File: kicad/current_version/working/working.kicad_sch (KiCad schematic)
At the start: 16 parts, among them J1 scuath, J1 sws2880, J1 swsi1h, J2 scumcsm, U1 imsp10mpump21rs2227

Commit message: workings
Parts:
- removed J1: swsi1h, oomlout_oomp_part_footprints:swsi1h_electronic_switch_slide_2d54_header_single_pole_double_throw, symbol oomlout_oomp_part_symbols:swsi1h_electronic_switch_slide_2d54_header_single_pol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
- removed J1: scuath, oomlout_oomp_part_footprints:scuath_electronic_socket_usb_a_through_hole, symbol oomlout_oomp_part_symbols:scuath_electronic_socket_usb_a_through_hole
- removed J1: sws2880, oomlout_oomp_part_footprints:sws2880_electronic_switch_slide_2_8_mm_x_8_mm_x_1_4_single_pole_double_throw, symbol oomlout_oomp_part_symbols:sws2880_electronic_switch_slide_2_8_mm_x_8_mm_x_1_4_s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
- removed J2 (x2): scumcsm, oomlout_oomp_part_footprints:scumcsm_electronic_socket_usb_micro_surface_mount, symbol oomlout_oomp_part_symbols:scumcsm_electronic_socket_usb_micro_surface_mount
- removed U1: imsp10mpump21rs2227, oomlout_oomp_part_footprints:imsp10mpump21rs2227_electronic_ic_msop_10_multiplexer_usb_multiplexer_two_to_one_jiangsu_r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, symbol oomlout_oomp_part_symbols:imsp10mpump21rs2227_electronic_ic_msop_10_multiplexer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
- added CON1 (x2): scumcsm, oomlout_oomp_part_footprints:scumcsm_electronic_socket_usb_micro_surface_mount, symbol oomlout_oomp_part_symbols:scumcsm_electronic_socket_usb_micro_surface_mount
- added CON1: scuath, oomlout_oomp_part_footprints:scuath_electronic_socket_usb_a_through_hole, symbol oomlout_oomp_part_symbols:scuath_electronic_socket_usb_a_through_hole
- added IC1: imsp10mpump21rs2227, oomlout_oomp_part_footprints:imsp10mpump21rs2227_electronic_ic_msop_10_multiplexer_usb_multiplexer_two_to_one_jiangsu_r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, symbol oomlout_oomp_part_symbols:imsp10mpump21rs2227_electronic_ic_msop_10_multiplexer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
- added SW1: swsi1h, oomlout_oomp_part_footprints:swsi1h_electronic_switch_slide_2d54_header_single_pole_double_throw, symbol oomlout_oomp_part_symbols:swsi1h_electronic_switch_slide_2d54_header_single_pol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
- added SW1: sws2880, oomlout_oomp_part_footprints:sws2880_electronic_switch_slide_2_8_mm_x_8_mm_x_1_4_single_pole_double_throw, symbol oomlout_oomp_part_symbols:sws2880_electronic_switch_slide_2_8_mm_x_8_mm_x_1_4_s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
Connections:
- net +5V: now also CON1.1 (VBUS), CON1.1 (VBUS), CON1.1 (VBUS), IC1.1 (___v_plus), SW1.2 (B), SW1.2 (B)
- net GND: now also CON1.4 (GND), CON1.5 (GND), CON1.5 (GND), CON1.5 (Shield), CON1.6 (Shield), CON1.6 (Shield), IC1.5 (___gnd)
- net usb_negative_main: now also CON1.2 (D-), IC1.4 (___d_minus)
- net usb_negative_secondary_1: now also CON1.2 (D-), IC1.6 (___hsd1_minus)
- net usb_negative_secondary_2: now also CON1.2 (D-), IC1.8 (___hsd2_minus)
- net usb_positive_main: now also CON1.3 (D+), IC1.3 (___d_plus)
- net usb_positive_secondary_1: now also CON1.3 (D+), IC1.7 (___hsd1_plus)
- net usb_positive_secondary_2: now also CON1.3 (D+), IC1.9 (___hsd2_plus)
- net at R1.1: now also IC1.10 (___oe)
- net out_1 renamed select
- net select: now also IC1.2 (___s), SW1.1 (A), SW1.1 (A)
- new net slide_switch_out_2: SW1.3 (C), SW1.3 (C)
- new net usb_id_secondary_1: CON1.4 (ID)
- new net usb_id_secondary_2: CON1.4 (ID)
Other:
- note added: "connector_usb_a_through_hole"
- note added: "connector_usb_micro_surface_mount"
- note added: "ic_usb_multiplexer_msop_10_two_to_one_rs2227xn"
- note added: "logic-glue"
- note added: "main"
- note added: "mechanical_board_shape_oobb_plate_03_03"
- note added: "oomp logic glue"
- note added: "rs2227 select"
- note added: "secondary_1"
- note added: "secondary_2"
- note added: "switch_slide_single_pole_double_throw_2_8_mm_x_8_mm_x_1_4"
- note added: "usb_a"
- note added: "usb_micro"
- note removed: "name"
- note removed: "oomp glue"
- note removed: "usb_a_main"
- note removed: "usb_micro secondary_1"
- note removed: "usb_micro secondary_2"

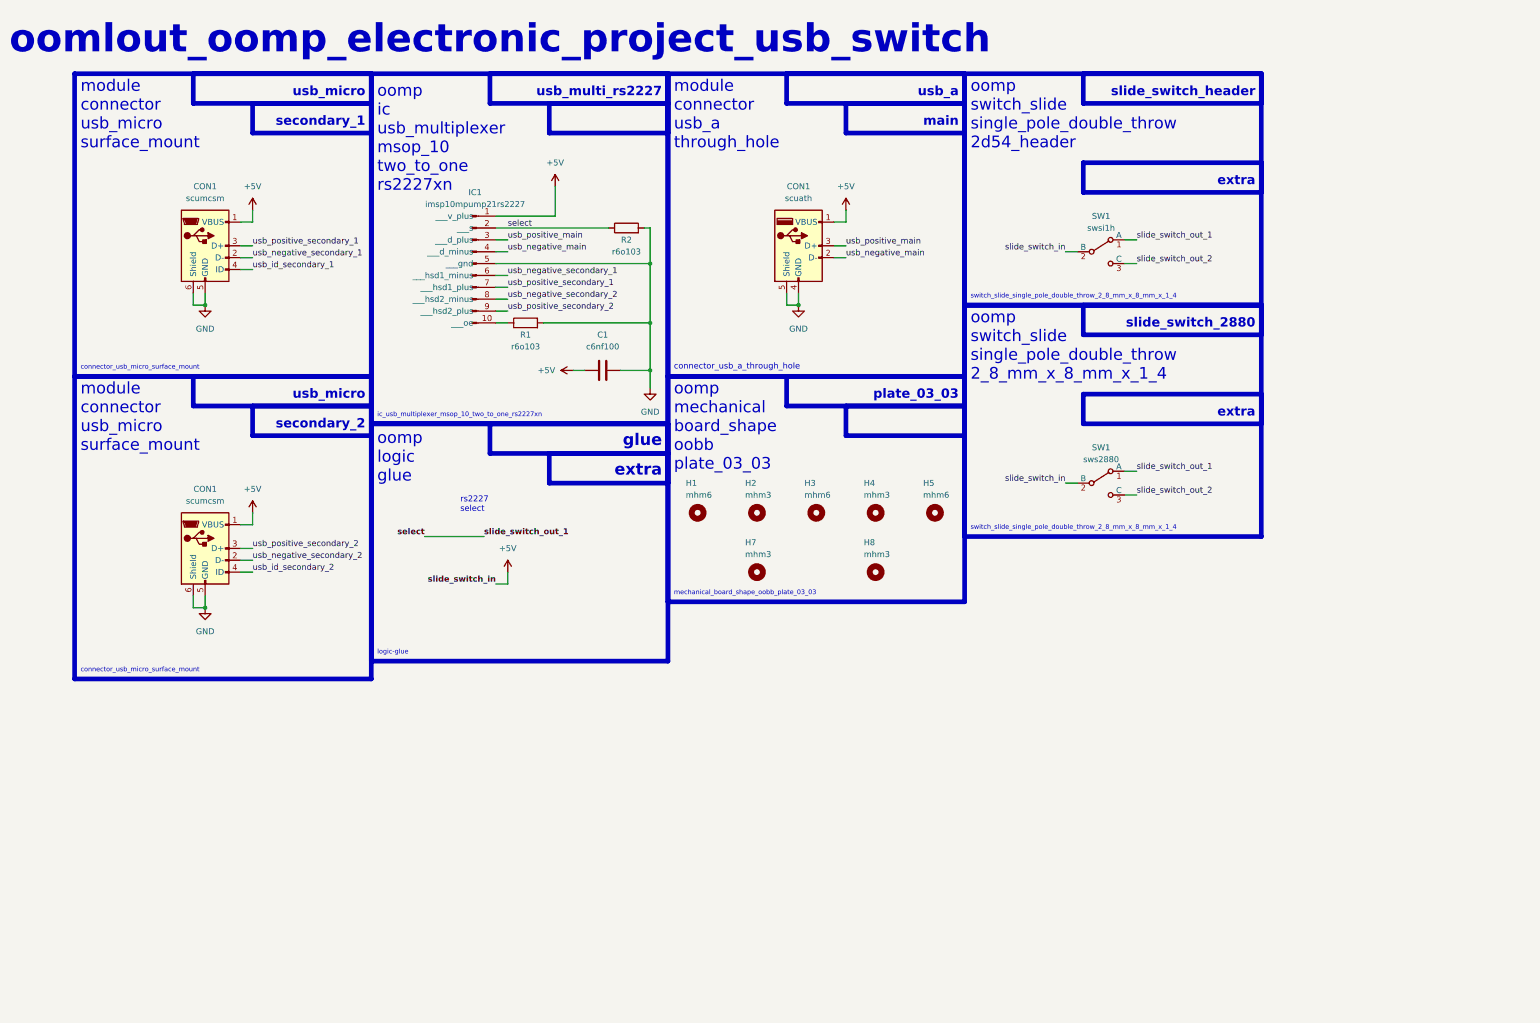
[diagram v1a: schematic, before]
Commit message: added power mux
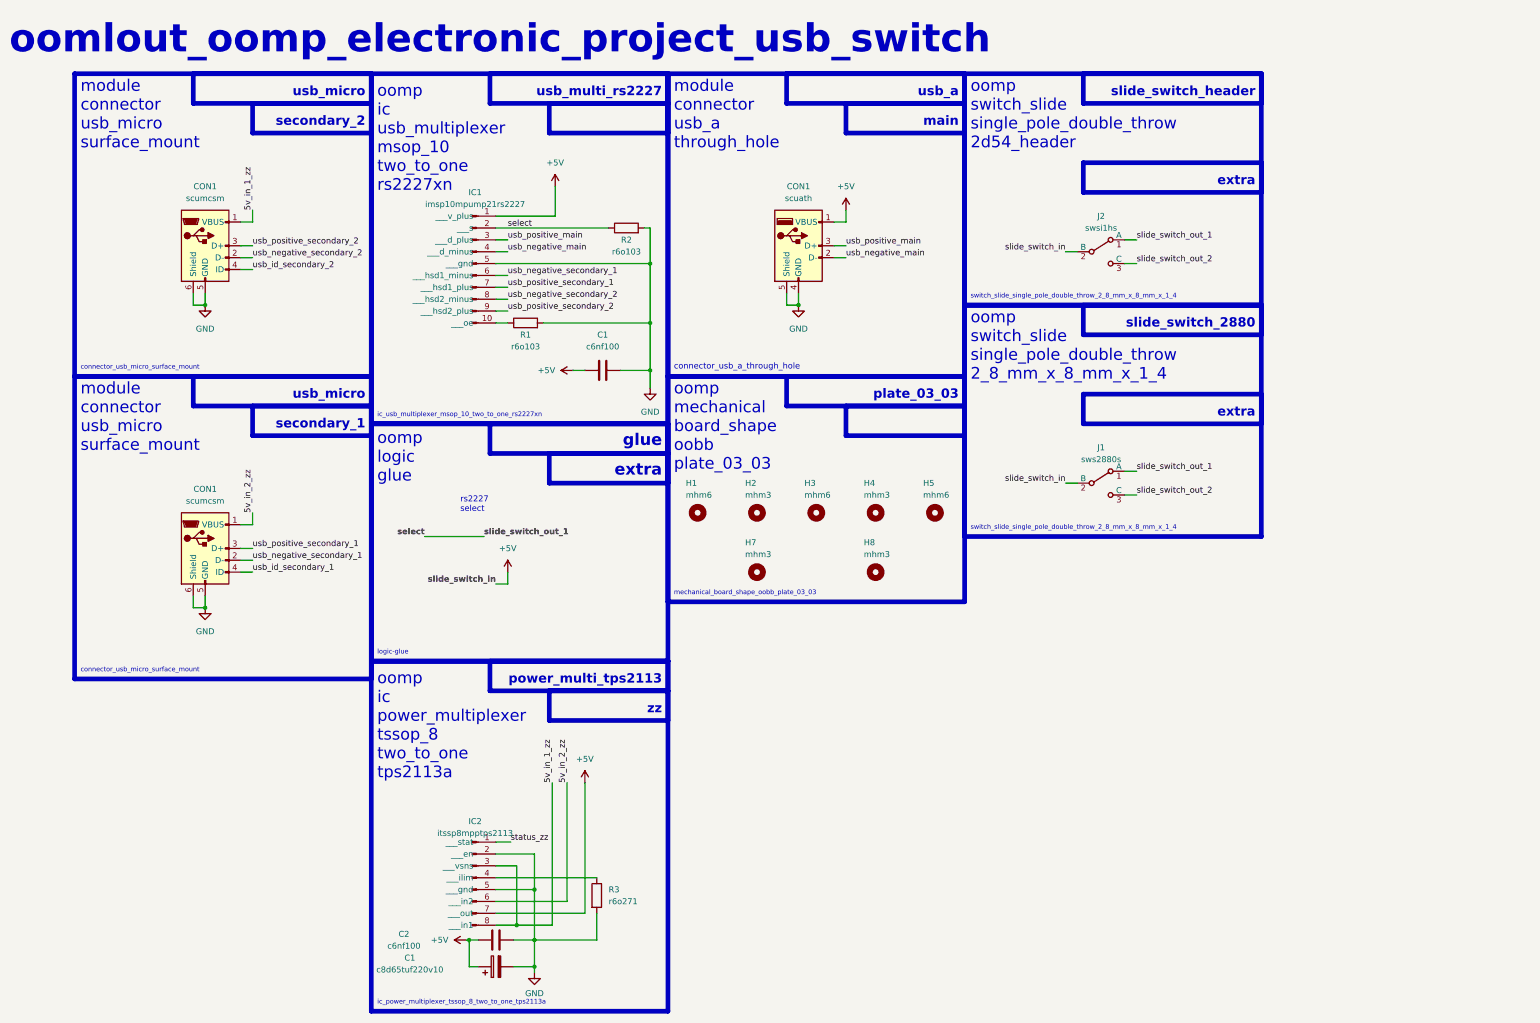
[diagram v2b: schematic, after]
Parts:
- removed SW1: swsi1h, oomlout_oomp_part_footprints:swsi1h_electronic_switch_slide_2d54_header_single_pole_double_throw, symbol oomlout_oomp_part_symbols:swsi1h_electronic_switch_slide_2d54_header_single_pol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
- removed SW1: sws2880, oomlout_oomp_part_footprints:sws2880_electronic_switch_slide_2_8_mm_x_8_mm_x_1_4_single_pole_double_throw, symbol oomlout_oomp_part_symbols:sws2880_electronic_switch_slide_2_8_mm_x_8_mm_x_1_4_s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
- added C1: c8d65tuf220v10, oomlout_oomp_part_footprints:c8d65tuf220v10_electronic_capacitor_8_mm_diameter_6_5_mm_tall_electrolytic_220_micro_farad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, symbol oomlout_oomp_part_symbols:c8d65tuf220v10_electronic_capacitor_8_mm_diameter_6_5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
- added C2: c6nf100, oomlout_oomp_part_footprints:c6nf100_electronic_capacitor_0603_100_nano_farad, symbol oomlout_oomp_part_symbols:c6nf100_electronic_capacitor_0603_100_nano_farad
- added IC2: itssp8mpptps2113, oomlout_oomp_part_footprints:itssp8mpptps2113_electronic_ic_tssop_8_multiplexer_power_multiplexer_texas_instruments_tps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, symbol oomlout_oomp_part_symbols:itssp8mpptps2113_electronic_ic_tssop_8_multiplexer_po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
- added J1: sws2880s, oomlout_oomp_part_footprints:sws2880s_electronic_switch_slide_2_8_mm_x_8_mm_x_1_4_mm_surface_mount_single_pole_double_t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, symbol oomlout_oomp_part_symbols:sws2880s_electronic_switch_slide_2_8_mm_x_8_mm_x_1_4_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
- added J2: swsi1hs, oomlout_oomp_part_footprints:swsi1hs_electronic_switch_slide_2d54_header_surface_mount_single_pole_double_throw, symbol oomlout_oomp_part_symbols:swsi1hs_electronic_switch_slide_2d54_header_surface_m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
- added R3: r6o271, oomlout_oomp_part_footprints:r6o271_electronic_resistor_0603_270_ohm, symbol oomlout_oomp_part_symbols:r6o271_electronic_resistor_0603_270_ohm
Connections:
- net +5V: now also C1.1, C2.1, IC2.7 (___out), J1.2 (B), J2.2 (B); no longer CON1.1 (VBUS), CON1.1 (VBUS)
- net GND: now also C1.2, C2.2, IC2.2 (___en), IC2.5 (___gnd), R3.2
- net select: now also J1.1 (A), J2.1 (A)
- net slide_switch_out_2: now also J1.3 (C), J2.3 (C)
- net usb_id_secondary_1: now also CON1.4 (ID); no longer CON1.4 (ID)
- net usb_id_secondary_2: now also CON1.4 (ID); no longer CON1.4 (ID)
- net usb_negative_secondary_1: now also CON1.2 (D-); no longer CON1.2 (D-)
- net usb_negative_secondary_2: now also CON1.2 (D-); no longer CON1.2 (D-)
- net usb_positive_secondary_1: now also CON1.3 (D+); no longer CON1.3 (D+)
- net usb_positive_secondary_2: now also CON1.3 (D+); no longer CON1.3 (D+)
- new net: IC2.4 (___ilim), R3.1
- new net 5v_in_1_zz: CON1.1 (VBUS), IC2.3 (___vsns), IC2.8 (___in1)
- new net 5v_in_2_zz: CON1.1 (VBUS), IC2.6 (___in2)
- new net status_zz: IC2.1 (___stat)
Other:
- note added: "ic_power_multiplexer_tssop_8_two_to_one_tps2113a"
- note added: "oomp ic power_multiplexer tssop_8 two_to_one tps2113a"
- note added: "power_multi_tps2113"
- note added: "zz"

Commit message: production update
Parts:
- added J1 (x3): hi14pth, oomlout_oomp_part_footprints:hi14pth_electronic_header_2_54_mm_4_pin_through_hole, symbol oomlout_oomp_part_symbols:hi14pth_electronic_header_2_54_mm_4_pin_through_hole
- SW2: renamed from J2; footprint oomlout_oomp_part_footprints:swsi1hs_electronic_switch_slide_2d54_header_surface_mount_single_pole_double_throw -> oomlout_oomp_part_footprints:swsi1hs_electronic_switch_slide_2_54_header_surface_mount_single_pole_double_throw
- renumbered J1 to SW1
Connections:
- net +5V: now also J1.1 (Pin_1)
- net 5v_in_1_zz: now also J1.1 (Pin_1)
- net 5v_in_2_zz: now also J1.1 (Pin_1)
- net GND: now also J1.4 (Pin_4), J1.4 (Pin_4), J1.4 (Pin_4)
- net usb_negative_main: now also J1.2 (Pin_2)
- net usb_negative_secondary_1: now also J1.2 (Pin_2)
- net usb_negative_secondary_2: now also J1.2 (Pin_2)
- net usb_positive_main: now also J1.3 (Pin_3)
- net usb_positive_secondary_1: now also J1.3 (Pin_3)
- net usb_positive_secondary_2: now also J1.3 (Pin_3)
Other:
- note added: "connector_usb_2d54_through_hole"
- note added: "connector_usb_2d_4_through_hole"
- note added: "oomp connector usb_2_54 through_hole"
- note added: "oomp connector usb_2d54 through_hole"
- note added: "oomp switch_slide single_pole_double_throw 2_54_header"
- note added: "usb_2d54"
- note removed: "oomp switch_slide single_pole_double_throw 2d54_header"
- moved on the sheet: C1, C2, CON1, H1, H2, H3, H4, H5, H7, H8, IC1, IC2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
